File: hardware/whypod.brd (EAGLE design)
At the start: 68.2 x 104.8 mm, 100 parts, among them IC1 IC_USBLC6-2, J1 AUDIO_JACK_TRRSSMD_RA, U1 USD-SOCKETUSD, X2 USB-A-S, Y2 CRYSTAL-GROUNDEDSMD-5X3.2

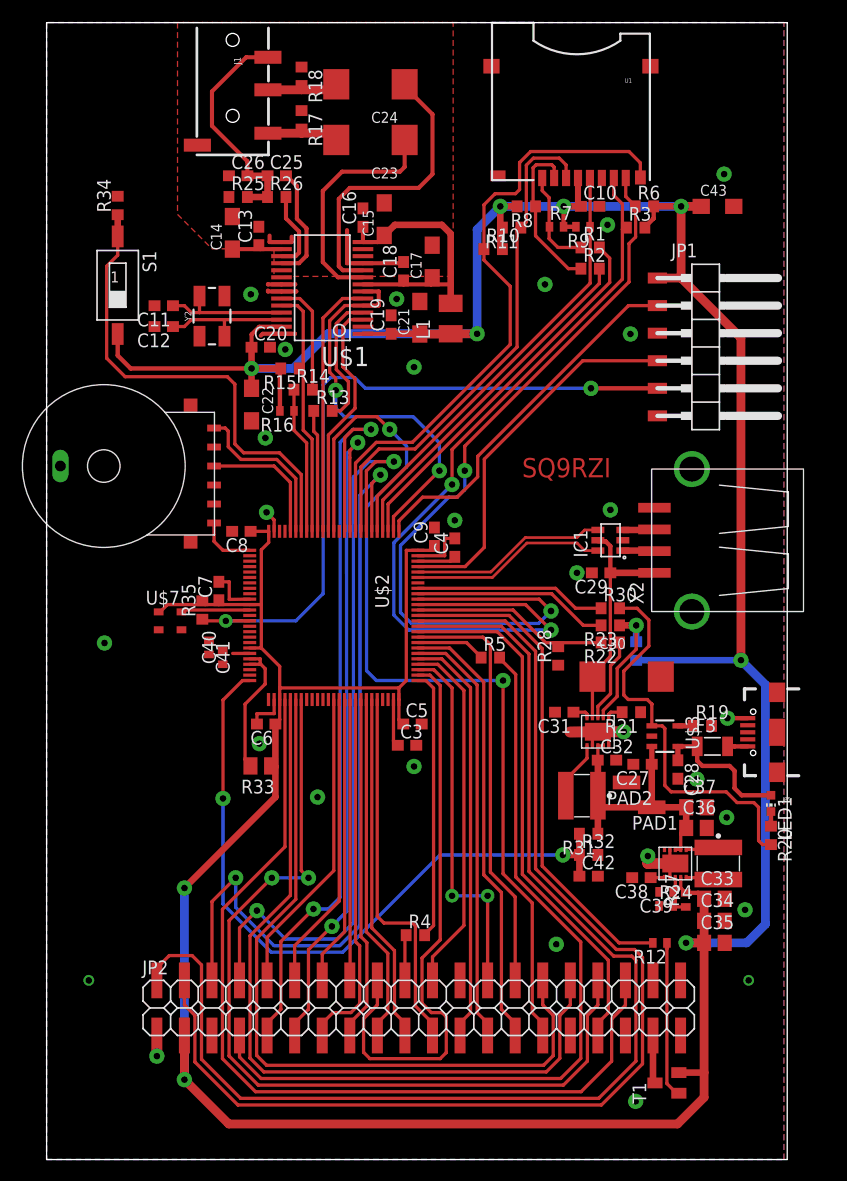
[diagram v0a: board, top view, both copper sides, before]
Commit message: Switches added
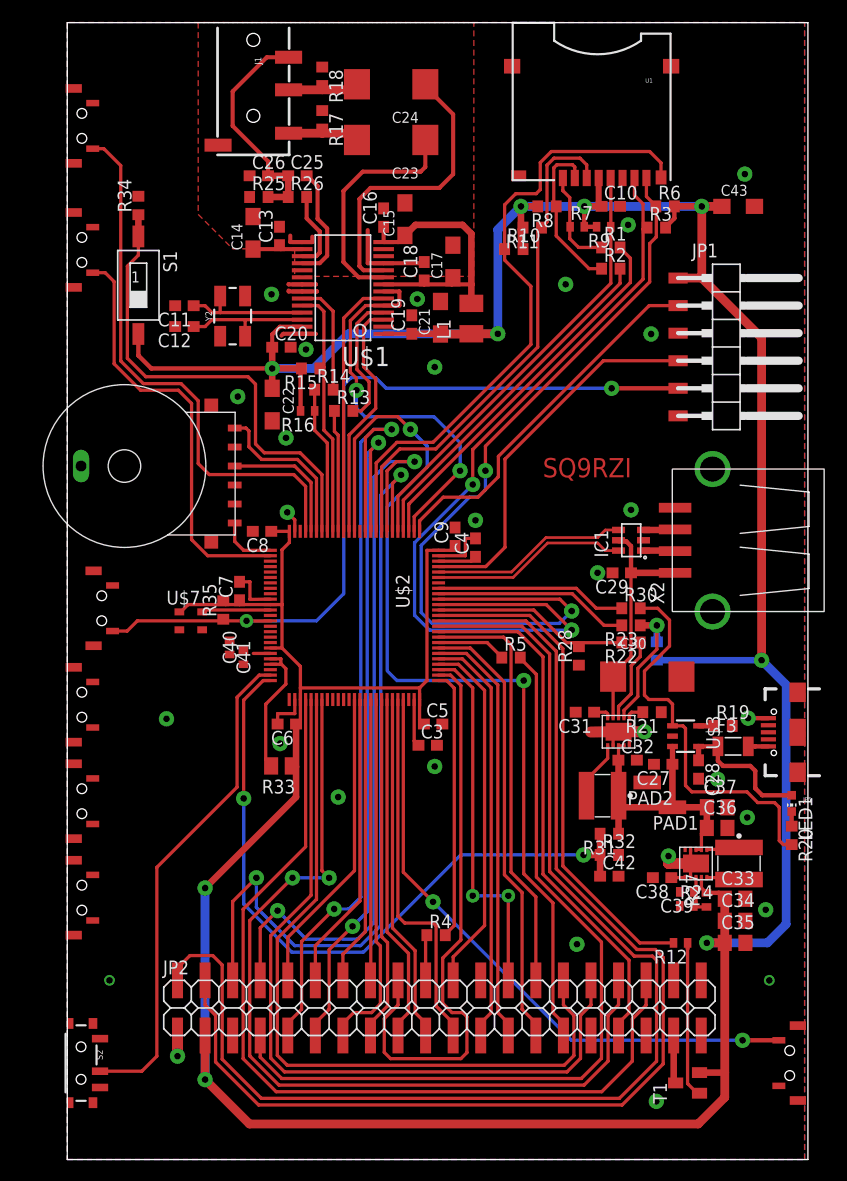
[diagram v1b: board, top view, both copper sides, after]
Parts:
- added S2: (no value), SparkFun-Switches:SWITCH_SPST_SMD_A
- added U$10, U$11, U$12, U$13, U$14, U$8, U$9: SMT3X6X3.5MM, mw:SMT3X6X3.5MM
- moved R35 1.93 mm to (14.4, 50.6)
- moved C10 1.91 mm to (50.1, 87.8)
- moved C13 1.91 mm to (19.6, 85.1)
- moved C16 1.91 mm to (29.2, 86.8)
- moved C18 1.91 mm to (32.9, 81.9)
- moved C19 1.91 mm to (31.8, 76.9)
- moved C20 1.91 mm to (19.7, 74.9)
- moved C22 1.91 mm to (18.9, 69.6)
- moved C25 1.91 mm to (21.2, 90.7)
- moved C27 1.91 mm to (54.9, 36.4)
- moved C29 1.91 mm to (51.1, 54.1)
- moved C3 1.91 mm to (33.2, 38.2)
- moved C30 1.91 mm to (53.5, 44.5)
- moved C31 1.91 mm to (47.7, 41.2)
- moved C32 1.91 mm to (51.6, 36.8)
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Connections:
- new net LOCK_SWITCH: S2.2, U$2.PA1
- new net PWR_BTN: U$2.PB10, U$8.A
- new net VOL_DN: U$10.A, U$2.PE3
- new net VOL_UP: U$2.PE0, U$9.A
- net GND: now also S2.3, U$10.B, U$10.MNT1, U$10.MNT2, U$11.B, U$11.MNT1, U$11.MNT2, U$12.B, U$12.MNT1, U$12.MNT2, U$13.B, U$13.MNT1, U$13.MNT2, U$14.B, U$14.MNT1, U$14.MNT2, U$8.B, U$8.MNT1, U$8.MNT2, U$9.B, U$9.MNT1, U$9.MNT2
- net NRST: now also U$14.A
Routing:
- net PWR_BTN: track 0.00 -> 56.9 mm, vias 0 -> 2
- net VOL_UP: track 0.00 -> 50.6 mm
- net LOCK_SWITCH: track 0.00 -> 45.9 mm
- net VOL_DN: track 0.00 -> 39.0 mm
- net NRST: track 65.2 -> 76.0 mm
- net GND: vias 26 -> 27

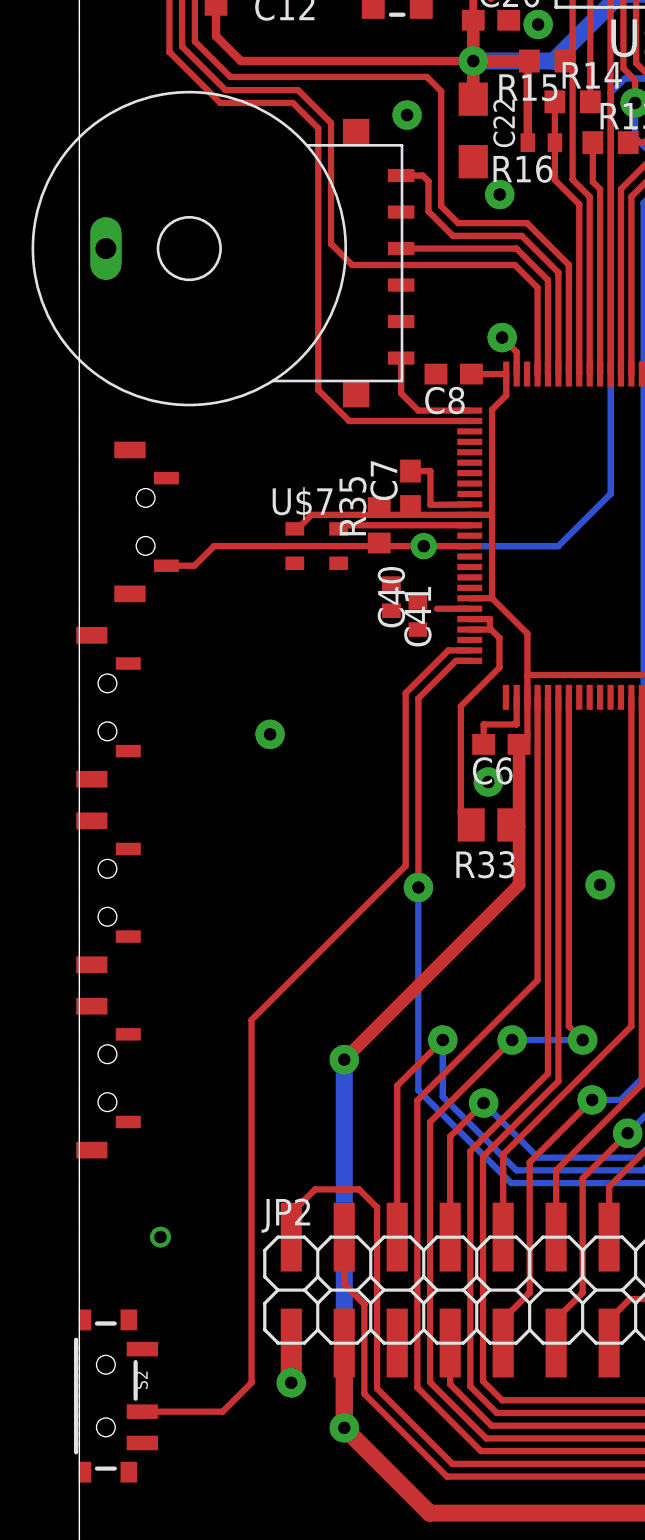
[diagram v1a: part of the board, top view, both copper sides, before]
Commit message: 32kHz oscillator added
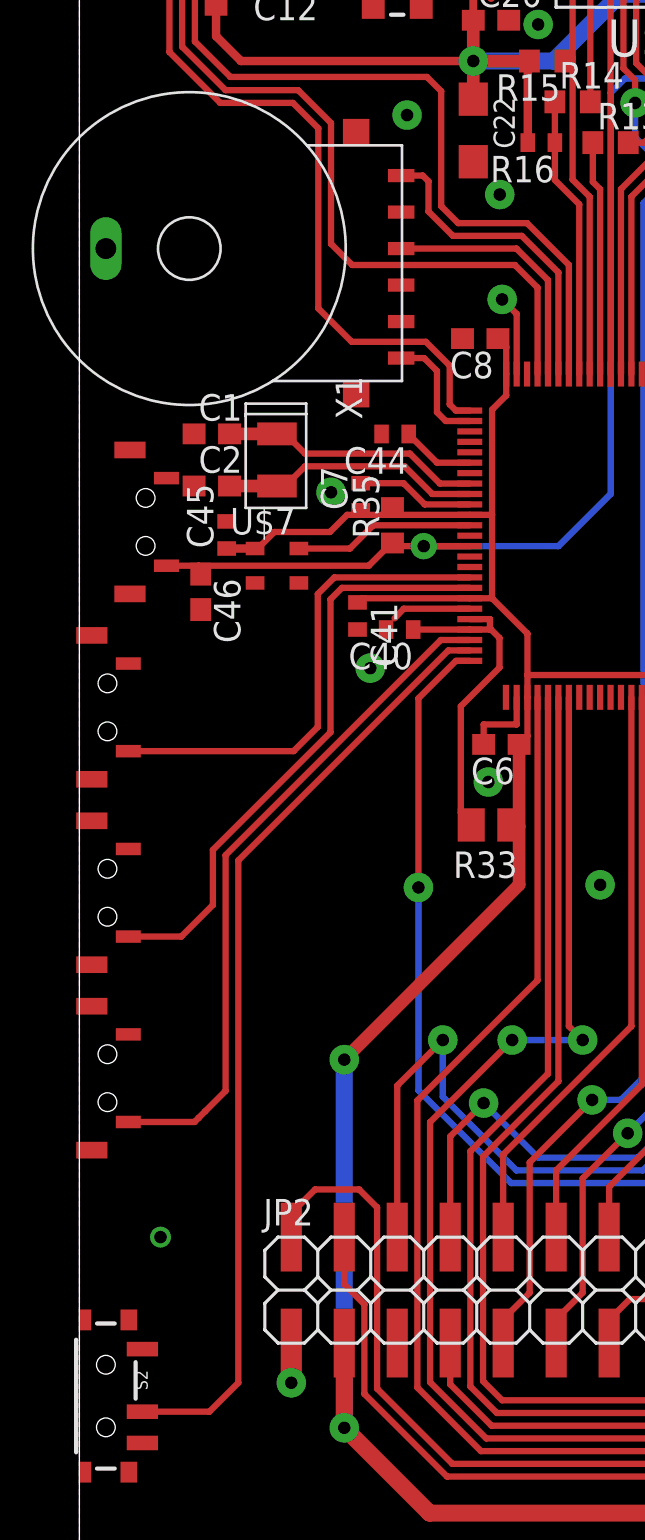
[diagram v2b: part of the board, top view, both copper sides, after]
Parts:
- added C1, C2, C46: (no value), rcl:C0603
- added C44, C45: (no value), rcl:C0402
- added X1: CRYSTALS-NOGND-CFPX-217, IQD-Frequency-Products:3.2X1.5-2-PAD
- C7: device rcl:C0603 -> rcl:C0402
- moved C7 2.42 mm to (13.5, 52.0)
- moved U$7 2.13 mm to (9.47, 48.7)
- moved C8 2.12 mm to (19.2, 59.6)
- moved C41 1.86 mm to (13.3, 46.3)
- moved C40 1.09 mm to (15.4, 45.6), turned to 180 degrees
- moved R35 0.63 mm to (15.0, 50.6)
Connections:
- new net KEY_1: U$11.A, U$2.PC2
- new net KEY_2: U$12.A, U$2.PC3
- new net KEY_3: U$13.A, U$2.PA0
- new net N$30: C44.1, U$2.VBAT
- new net OSC32_IN: C1.2, U$2.PC14, X1.1
- new net OSC32_OUT: C2.2, U$2.PC15, X1.2
- net 3V: now also C45.1
- net GND: now also C1.1, C2.1, C44.2, C45.2, C46.2
- net NRST: now also C46.1
- net SW_A: now also U$2.PE3; no longer U$2.PE2
- net VOL_DN: now also U$2.PE2; no longer U$2.PE3
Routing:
- net KEY_3: track 0.00 -> 32.6 mm
- net KEY_2: track 0.00 -> 28.6 mm
- net KEY_1: track 0.00 -> 23.6 mm
- net OSC32_IN: track 0.00 -> 12.5 mm
- net OSC32_OUT: track 0.00 -> 12.5 mm
- net 3V: track 381.3 -> 390.5 mm
- net GND: track 42.1 -> 47.4 mm, vias 27 -> 28
- net N$30: track 0.00 -> 3.51 mm
- net N$28: track 13.0 -> 15.7 mm
- net PH0: track 6.36 -> 8.65 mm
- net VOL_DN: track 39.0 -> 37.5 mm

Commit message: PCB updates
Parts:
- added C47: (no value), rcl:C0603
- added C48: (no value), rcl:SMC_A
- added R36, R37: 10k, rcl:R0603
- moved C3 1.32 mm to (33.2, 36.9)
- moved C5 1.32 mm to (33.7, 38.8)
- moved R30 1.30 mm to (51.9, 52.1)
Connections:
- removed net SWD_SWO: JP1.6
- new net UART1_TX: JP1.6, U$2.PA9
- net 3V: now also C48.+, R36.1, R37.1
- net CHARGING: now also U$2.PA10; no longer U$2.PA9
- net GND: now also C47.2, C48.-
- net N$28: now also C47.1
- net SD_CS: now also R36.2
- net T_CS: now also R37.2
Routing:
- net UART1_TX: track 0.00 -> 50.9 mm, vias 0 -> 2
- net 3V: track 390.5 -> 397.2 mm
- net N$6: track 4.38 -> 5.70 mm
- net N$18: track 36.3 -> 37.6 mm
- net ADC1_IN2: track 64.3 -> 65.4 mm
- net GND: vias 28 -> 29

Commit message: Some updates
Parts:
- moved U$14 0.25 mm to (2.92, 50.8)
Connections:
- net GND: now also X2.P$5, X2.P$6
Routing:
- net UART1_TX: track 50.9 -> 48.9 mm
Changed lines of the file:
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@@
 <rectangle x1="59.69761875" y1="26.035" x2="64.0969" y2="28.575" layer="41"/>
 <rectangle x1="48.26" y1="31.3309" x2="50.2666" y2="35.72255625" layer="41"/>
+<circle x="64.69" y="102.235" radius="1.778" width="0.254" layer="41"/>
+<circle x="3.89" y="102.235" radius="1.778" width="0.254" layer="41"/>
+<circle x="3.89" y="102.235" radius="1.778" width="0.254" layer="42"/>
+<circle x="64.69" y="102.235" radius="1.778" width="0.254" layer="42"/>
+<circle x="3.89" y="16.51" radius="1.778" width="0.254" layer="42"/>
+<circle x="64.69" y="16.51" radius="1.778" width="0.254" layer="42"/>
 </plain>
 <attributes>
@@
 <element name="U$12" library="mw" package="SMT3X6X3.5MM" value="SMT3X6X3.5MM" x="1.3462" y="33.02" rot="R90"/>
 <element name="U$13" library="mw" package="SMT3X6X3.5MM" value="SMT3X6X3.5MM" x="1.3462" y="24.13" rot="R90"/>
-<element name="U$14" library="mw" package="SMT3X6X3.5MM" value="SMT3X6X3.5MM" x="3.175" y="50.8" rot="R90"/>
+<element name="U$14" library="mw" package="SMT3X6X3.5MM" value="SMT3X6X3.5MM" x="2.921" y="50.8" rot="R90"/>
 <element name="S2" library="SparkFun-Switches" package="SWITCH_SPST_SMD_A" value="" x="1.27" y="8.89" rot="R90">
 <attribute name="SF_SKU" value="COM-10860" x="1.27" y="8.89" size="1.778" layer="27" rot="R90" display="off"/>
@@
 <contactref element="C48" pad="-"/>
 <via x="16.637" y="36.2712" extent="1-16" drill="0.6" diameter="1.4224" shape="octagon"/>
+<contactref element="X2" pad="P$6"/>
+<contactref element="X2" pad="P$5"/>
 </signal>
 <signal name="DB0">
@@
 <wire x1="15.0114" y1="49.7896" x2="15.09" y2="49.7896" width="0.3048" layer="1"/>
 <wire x1="15.09" y1="49.7896" x2="15.24" y2="49.6396" width="0.3048" layer="1"/>
-<wire x1="4.175" y1="48.7" x2="5.715" y2="48.7" width="0.3048" layer="1"/>
+<wire x1="3.921" y1="48.7" x2="5.715" y2="48.7" width="0.3048" layer="1"/>
 <wire x1="5.715" y1="48.7" x2="13.8766" y2="48.7" width="0.3048" layer="1"/>
 <wire x1="13.8766" y1="48.7" x2="14.9662" y2="49.7896" width="0.3048" layer="1"/>
@@
 <wire x1="22.5806" y1="84.545" x2="22.5806" y2="85.0392" width="0.381" layer="1"/>
 </signal>
+<signal name="N$32">
+<via x="64.69" y="16.51" extent="1-16" drill="0.6"/>
+</signal>
 <signal name="N$9">
-<via x="64.69" y="16.51" extent="1-16" drill="0.6"/>
+<via x="64.69" y="102.235" extent="1-16" drill="0.6"/>
+</signal>
+<signal name="N$31">
+<via x="3.89" y="16.51" extent="1-16" drill="0.6"/>
 </signal>
 <signal name="N$10">
-<via x="3.89" y="16.51" extent="1-16" drill="0.6"/>
+<via x="3.89" y="102.235" extent="1-16" drill="0.6"/>
 </signal>
 <signal name="I2S_WS">
@@
 <wire x1="50.0126" y1="50.6476" x2="48.895" y2="50.6476" width="0.3048" layer="1"/>
 <via x="54.4068" y="52.0954" extent="1-16" drill="0.6" diameter="1.4224" shape="octagon"/>
-<wire x1="62.865" y1="67.31" x2="61.6458" y2="68.5292" width="0.3048" layer="1"/>
+<wire x1="62.23" y1="66.675" x2="60.3758" y2="68.5292" width="0.3048" layer="1"/>
 <contactref element="JP1" pad="6"/>
-<wire x1="56.2864" y1="68.5292" x2="61.6458" y2="68.5292" width="0.3048" layer="1"/>
+<wire x1="56.2864" y1="68.5292" x2="60.3758" y2="68.5292" width="0.3048" layer="1"/>
 <wire x1="54.4068" y1="52.0954" x2="51.4604" y2="52.0954" width="0.4064" layer="16"/>
 <wire x1="51.4604" y1="52.0954" x2="50.0126" y2="50.6476" width="0.4064" layer="16"/>
-<wire x1="55.4482" y1="53.1368" x2="61.3918" y2="53.1368" width="0.3048" layer="1"/>
-<wire x1="61.3918" y1="53.1368" x2="62.865" y2="54.61" width="0.3048" layer="1"/>
+<wire x1="55.4482" y1="53.1368" x2="60.1218" y2="53.1368" width="0.3048" layer="1"/>
 <wire x1="54.4068" y1="52.0954" x2="55.4482" y2="53.1368" width="0.3048" layer="1"/>
-<wire x1="62.865" y1="54.61" x2="62.865" y2="67.31" width="0.3048" layer="1"/>
+<wire x1="62.23" y1="55.245" x2="62.23" y2="66.675" width="0.3048" layer="1"/>
+<wire x1="60.1218" y1="53.1368" x2="62.23" y2="55.245" width="0.3048" layer="1"/>
 </signal>
 </signals>
